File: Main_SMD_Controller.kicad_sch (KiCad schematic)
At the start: 59 parts, among them J1 2.1-5.5 +12VDC, J10 Vin_-, J11 Conn_01x02, J12 Vsens, J13 Vin+, J2 Switch_Control, J3 +5V, J4 AnalogIO, J5 +12V, J6 VsensJMP, J7 Drain, J8 Gate, J9 Source, P1 Eoshi-chan_Silk, P2 Eoshi-chan_Silk, P3 Serial_QR, Q1 2N7002K, U1 NJW4191M, U2 NJM7805SDL1, U3 TC74HC4066AP, U4 AD8226ARZ, U5 S-89713B-K8T2U

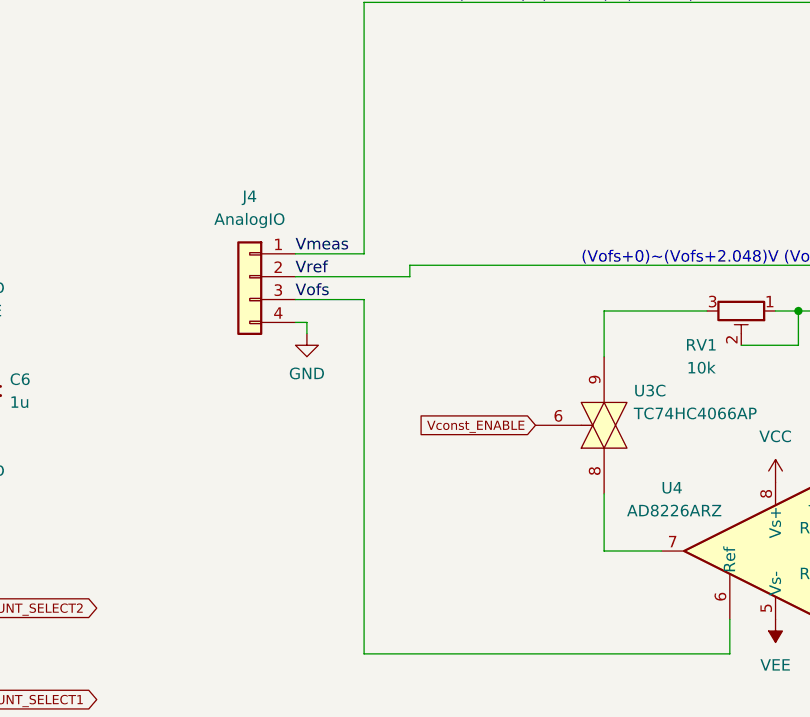
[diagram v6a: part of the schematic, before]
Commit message: 4 layered
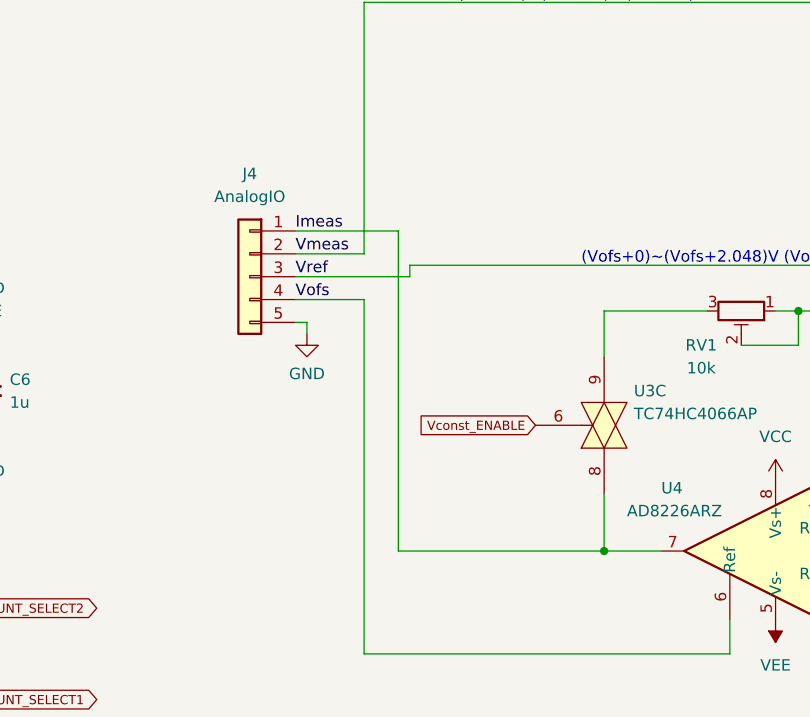
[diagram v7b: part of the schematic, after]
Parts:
- J4: footprint Connector_JST:JST_XH_B4B-XH-A_1x04_P2.50mm_Vertical -> Connector_JST:JST_XH_B5B-XH-A_1x05_P2.50mm_Vertical; symbol Connector_Generic:Conn_01x04 -> Connector_Generic:Conn_01x05
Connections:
- net GND: now also J4.5 (Pin_5); no longer J4.4 (Pin_4)
- net Vmeas: now also J4.2 (Pin_2); no longer J4.1 (Pin_1)
- net Vofs: now also J4.4 (Pin_4); no longer J4.3 (Pin_3)
- net Vref: now also J4.3 (Pin_3); no longer J4.2 (Pin_2)
- net Imeas: now reaches U3.8, U4.7
- net Imeas: now also J4.1 (Pin_1)
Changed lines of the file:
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@@
 	)
 	(junction
+		(at 143.51 111.76)
+		(diameter 0)
+		(color 0 0 0 0)
+	)
+	(junction
 		(at 214.63 135.89)
 		(diameter 0)
@@
 	(wire
 		(pts
+			(xy 120.65 76.2) (xy 109.22 76.2)
+		)
+		(stroke
+			(width 0)
+			(type default)
+		)
+	)
+	(wire
+		(pts
 			(xy 173.99 30.48) (xy 173.99 36.83)
 		)
@@
 	(wire
 		(pts
+			(xy 143.51 111.76) (xy 120.65 111.76)
+		)
+		(stroke
+			(width 0)
+			(type default)
+		)
+	)
+	(wire
+		(pts
 			(xy 251.46 50.8) (xy 251.46 39.37)
 		)
@@
 	(wire
 		(pts
+			(xy 120.65 111.76) (xy 120.65 76.2)
+		)
+		(stroke
+			(width 0)
+			(type default)
+		)
+	)
+	(wire
+		(pts
 			(xy 52.07 157.48) (xy 60.96 157.48)
 		)
@@
 		)
 	)
+	(label "Imeas"
+		(at 109.22 76.2 0)
+		(effects
+			(font
+				(size 1.27 1.27)
+			)
+			(justify left bottom)
+		)
+	)
 	(label "TH_1"
 		(at 259.08 92.71 90)
@@
 	)
 	(symbol
-		(lib_id "Connector_Generic:Conn_01x04")
+		(lib_id "Connector_Generic:Conn_01x05")
 		(at 104.14 81.28 0)
 		(mirror y)
@@
 		(fields_autoplaced yes)
 		(property "Reference" "J4"
-			(at 104.14 72.39 0)
+			(at 104.14 69.85 0)
 			(effects
 				(font
@@
 		)
 		(property "Value" "AnalogIO"
-			(at 104.14 74.93 0)
+			(at 104.14 72.39 0)
 			(effects
 				(font
@@
 			)
 		)
-		(property "Footprint" "Connector_JST:JST_XH_B4B-XH-A_1x04_P2.50mm_Vertical"
+		(property "Footprint" "Connector_JST:JST_XH_B5B-XH-A_1x05_P2.50mm_Vertical"
 			(at 104.14 81.28 0)
 			(effects
@@
 			)
 		)
-		(property "Datasheet" "https://akizukidenshi.com/goodsaffix/xh.pdf"
+		(property "Datasheet" "~"
 			(at 104.14 81.28 0)
 			(effects
@@
 			)
 		)
-		(property "Description" ""
+		(property "Description" "Generic connector, single row, 01x05, script generated (kicad-library-utils/schlib/autogen/connector/)"
 			(at 104.14 81.28 0)
 			(effects
@@
 					(size 1.27 1.27)
 				)
+				(hide yes)
 			)
 		)
@@
 		(pin "4"
 		)
+		(pin "5"
+		)
 		(instances

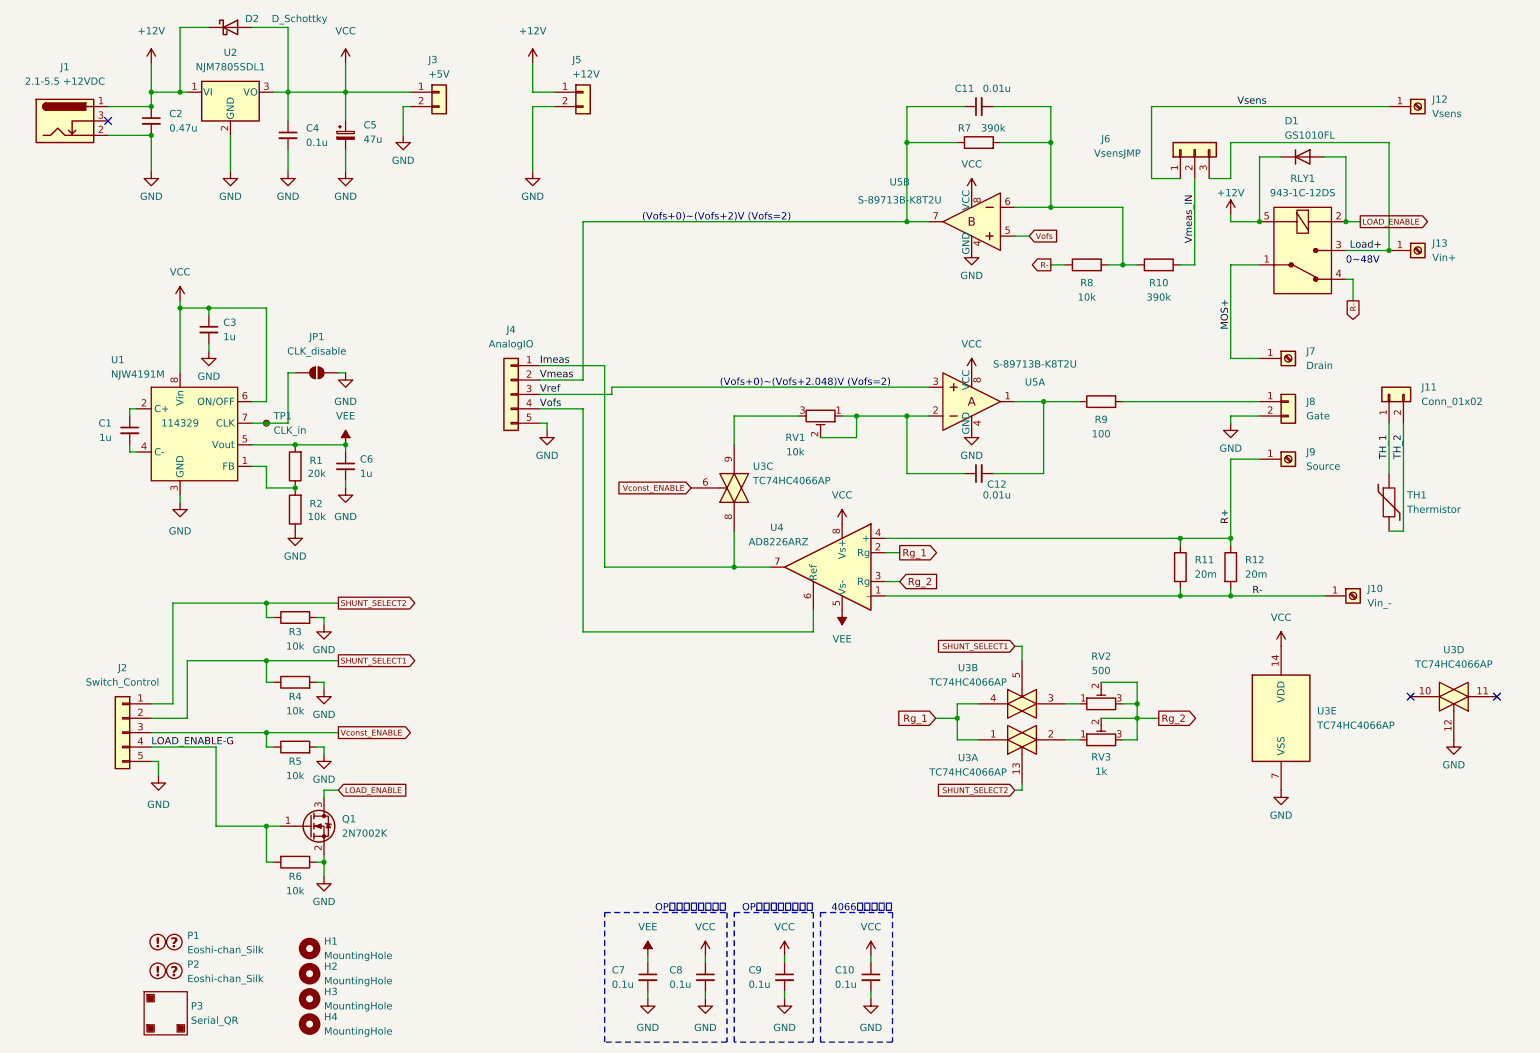
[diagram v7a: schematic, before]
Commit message: fix voltage measure circuit
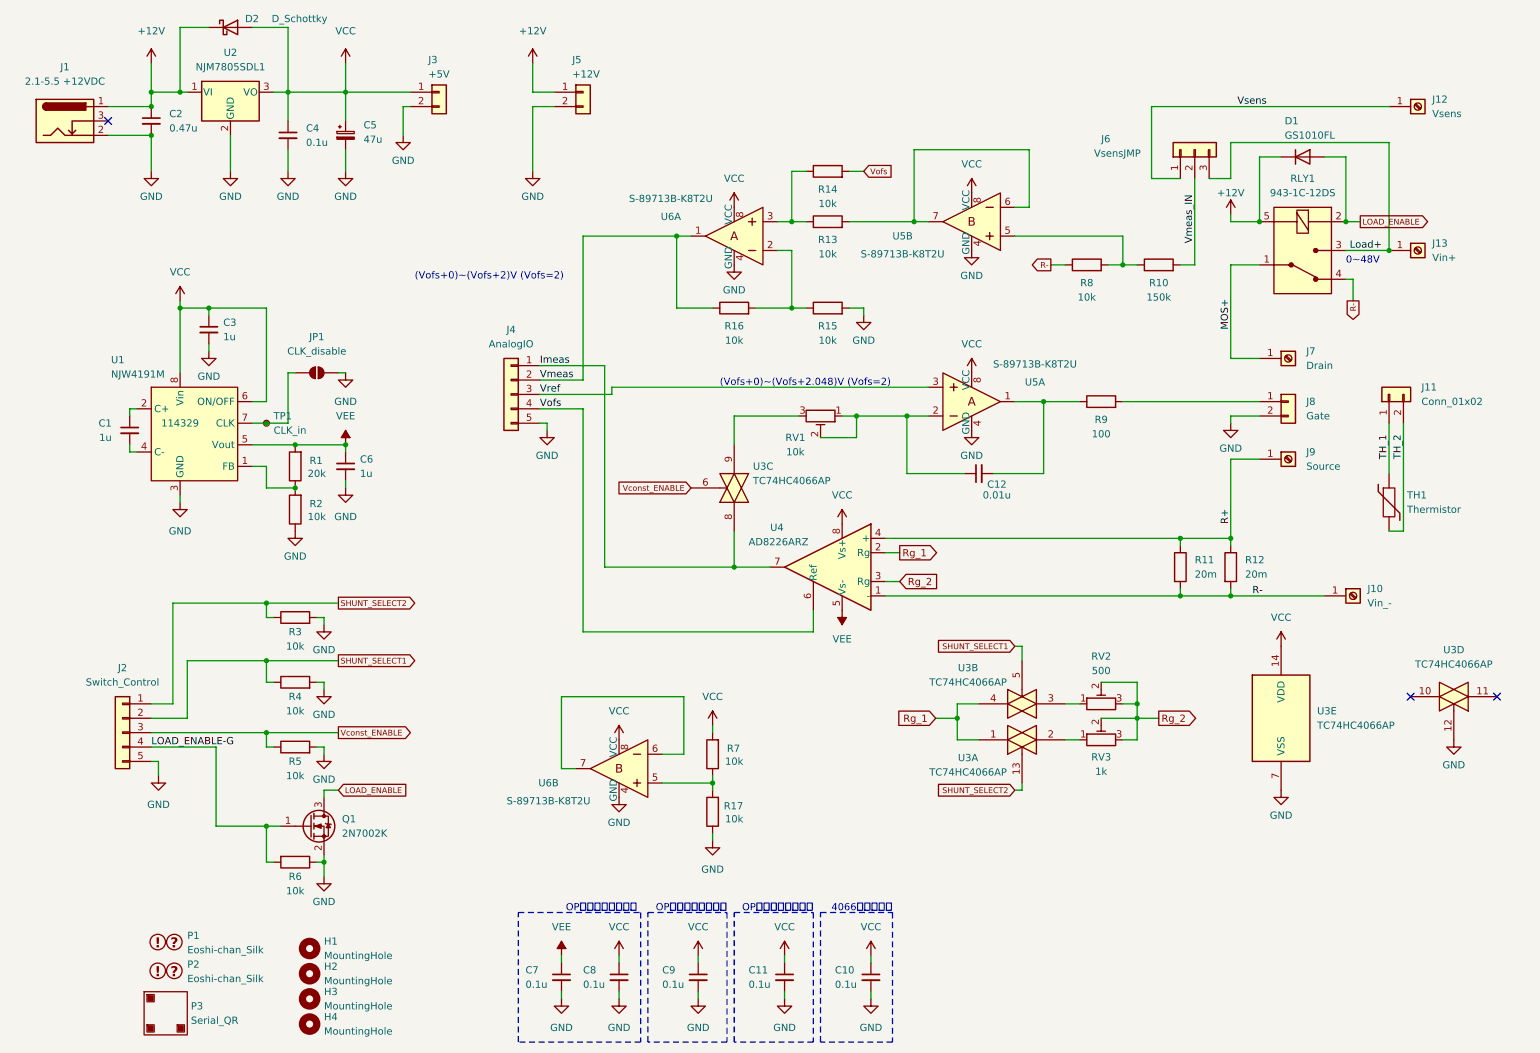
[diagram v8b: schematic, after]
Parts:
- added R13, R14, R15, R16, R17: 10k, Resistor_SMD:R_0603_1608Metric, symbol Device:R
- added U6: S-89713B-K8T2U, Package_SO:MSOP-8_3x3mm_P0.65mm, symbol dk_Linear-Amplifiers-Instrumentation-OP-Amps-Buffer-Amps:LM358N_Obsolete
- C11: value 0.01u -> 0.1u; footprint Capacitor_SMD:C_0402_1005Metric -> Capacitor_SMD:C_0603_1608Metric; Akizuki_code 116112 -> 116143
- R10: value 390k -> 150k
- R7: value 390k -> 10k; footprint Resistor_THT:R_Axial_DIN0207_L6.3mm_D2.5mm_P5.08mm_Vertical -> Resistor_SMD:R_0603_1608Metric
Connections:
- net GND: now also C11.2, R15.2, R17.1, U6.4 (GND), U6.4 (GND)
- net VCC: now also C11.1, R7.2, U6.8 (VCC), U6.8 (VCC)
- net Vmeas: now also R16.1, U6.1; no longer C11.1, R7.1, U5.7
- net Vofs: now also R14.2; no longer U5.5
- new net: R13.1, R14.1, U6.3
- new net: R13.2, U5.6, U5.7
- new net: R15.1, R16.2, U6.2
- new net: R10.1, R8.2, U5.5
- new net: R17.2, R7.1, U6.5
- new net: U6.6, U6.7
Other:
- moved on the sheet: C7, C8, C9
